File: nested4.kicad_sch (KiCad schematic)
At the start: 3 parts, among them J2 54-00285

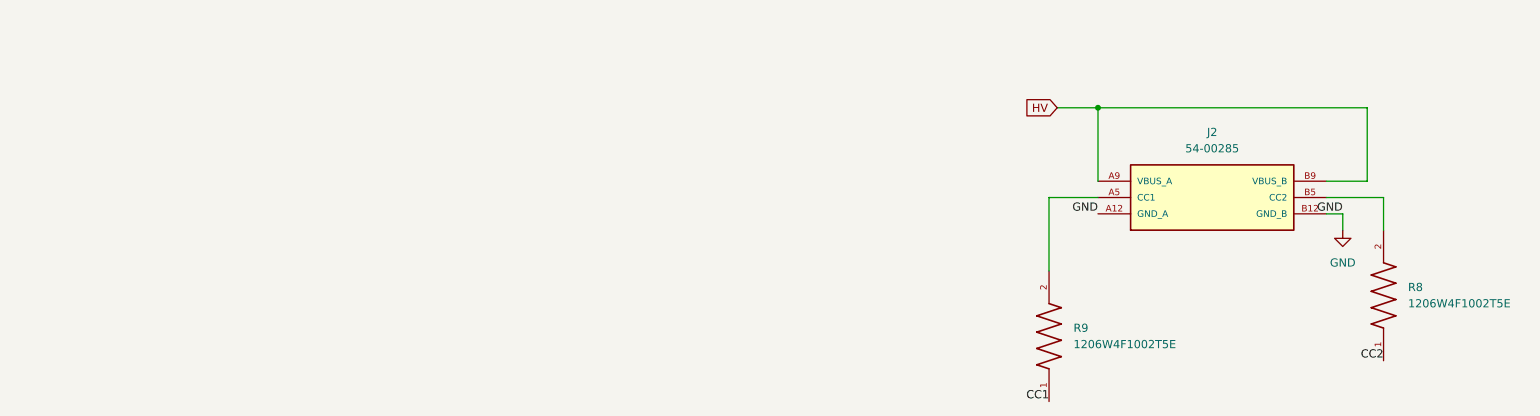
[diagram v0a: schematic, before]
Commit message: footprints added and usb cct finished
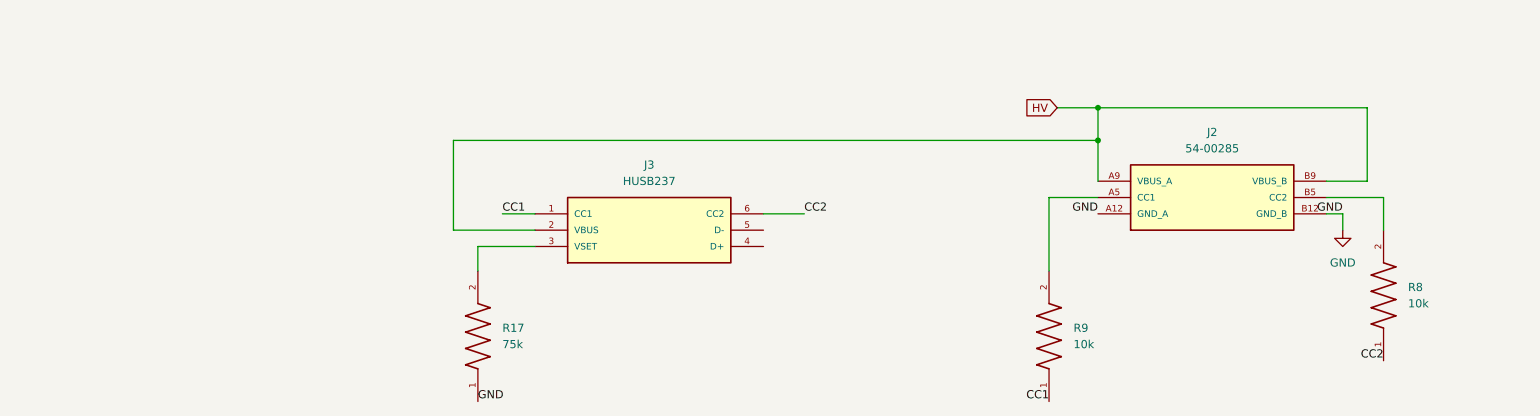
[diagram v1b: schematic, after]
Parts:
- added J3: HUSB237, Package_DFN_QFN:DFN-6-1EP_2x2mm_P0.65mm_EP1x1.6mm, symbol 54-00285[1]:54-00285
- added R17: 75k, Resistor_SMD:R_1206_3216Metric_Pad1.30x1.75mm_HandSolder, symbol 1206W4F1002T5E[1]:1206W4F1002T5E
- J2: footprint 54-00285:TENSILITY_54-00285 -> Connector_USB:USB_C_Receptacle_HRO_TYPE-C-31-M-17
- R8: value 1206W4F1002T5E -> 10k; footprint 1206W4F1002T5E:RESC3115X65N -> Resistor_SMD:R_1206_3216Metric_Pad1.30x1.75mm_HandSolder
- R9: value 1206W4F1002T5E -> 10k
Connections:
- net CC1: now also J3.1 (CC1)
- net CC2: now also J3.6 (CC2)
- net GND: now also R17.1
- net HV: now also J3.2 (VBUS)
- new net: J3.3 (VSET), R17.2

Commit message: added LCSC numbers and finsihed footprints
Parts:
- J2: LCSC (none) -> C456012
- J3: LCSC (none) -> C22373734
- R17: LCSC (none) -> C23242
- R8, R9: LCSC (none) -> C17902
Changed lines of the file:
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@@
+			)
+		)
+		(property "LCSC" "C22373734"
+			(at 115.57 100.33 0)
+			(effects
+				(font
+					(size 1.27 1.27)
+				)
+				(hide yes)
 			)
 		)
@@
 			)
 		)
+		(property "LCSC" "C17902"
+			(at 177.8 96.52 90)
+			(effects
+				(font
+					(size 1.27 1.27)
+				)
+				(hide yes)
+			)
+		)
 		(pin "1"
 		)
@@
 			)
 		)
+		(property "LCSC" "C456012"
+			(at 203.2 74.93 0)
+			(effects
+				(font
+					(size 1.27 1.27)
+				)
+				(hide yes)
+			)
+		)
 		(pin "B9"
 		)
@@
 			)
 		)
+		(property "LCSC" "C17902"
+			(at 229.87 90.17 90)
+			(effects
+				(font
+					(size 1.27 1.27)
+				)
+				(hide yes)
+			)
+		)
 		(pin "1"
 		)
@@
 				(hide yes)
 			)
+		)
+		(property "LCSC" "C23242"
+			(at 88.9 96.52 90)
+			(effects
+				(font
+					(size 1.27 1.27)
+				)
+				(hide yes)
+			)

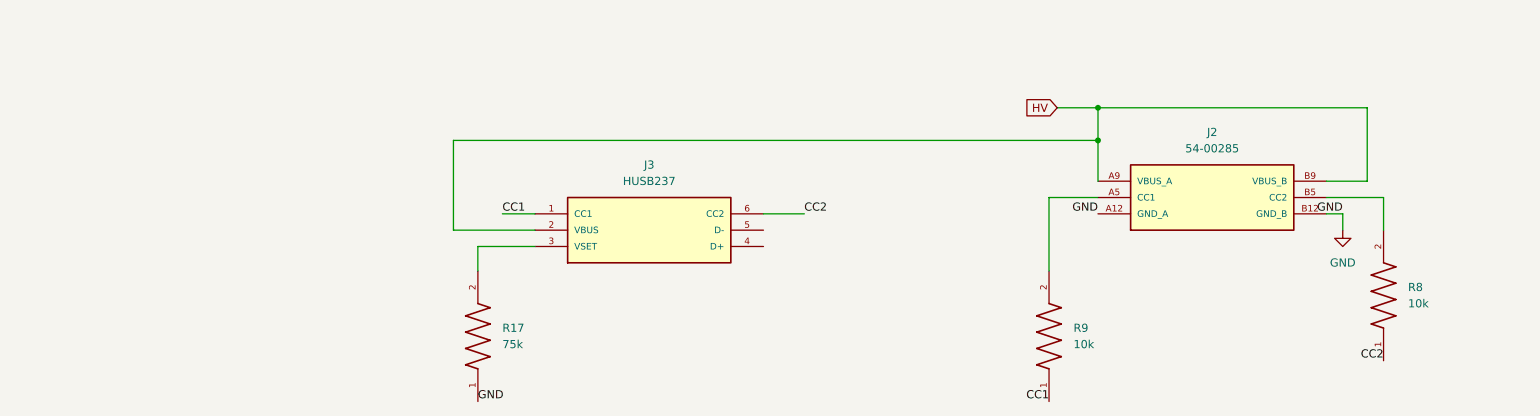
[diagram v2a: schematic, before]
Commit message: Removed old backups and updated KiCad files
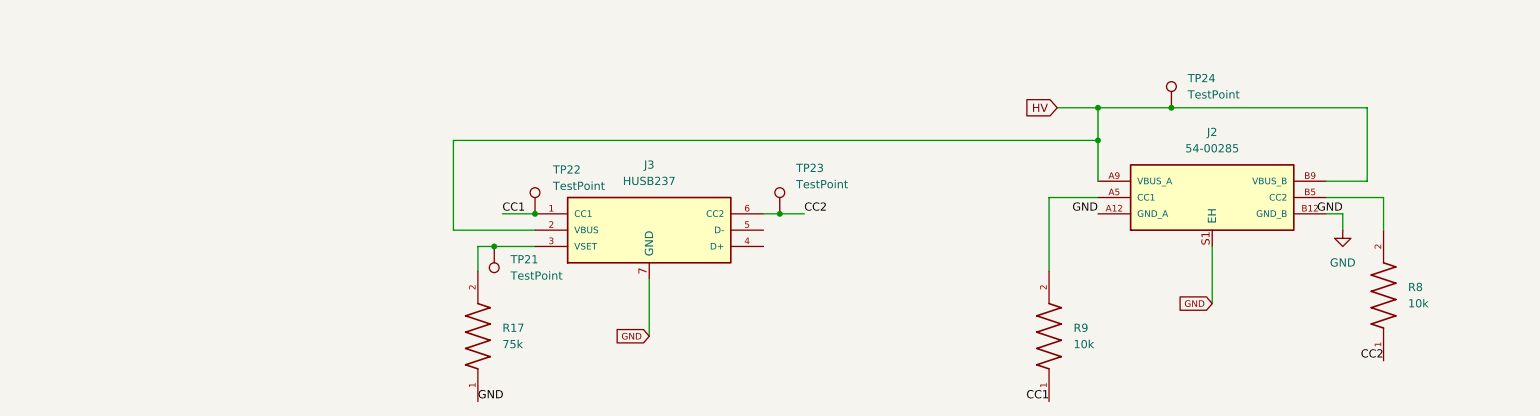
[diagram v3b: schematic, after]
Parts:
- added TP21, TP22, TP23, TP24: TestPoint, TestPoint:TestPoint_Pad_1.0x1.0mm, symbol Connector:TestPoint
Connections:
- net CC1: now also TP22.1
- net CC2: now also TP23.1
- net GND: now also J2.S1 (EH), J3.7 (GND)
- net HV: now also TP24.1
- net at J3.3 (VSET), R17.2: now also TP21.1

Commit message: Removed old backups and updated KiCad files
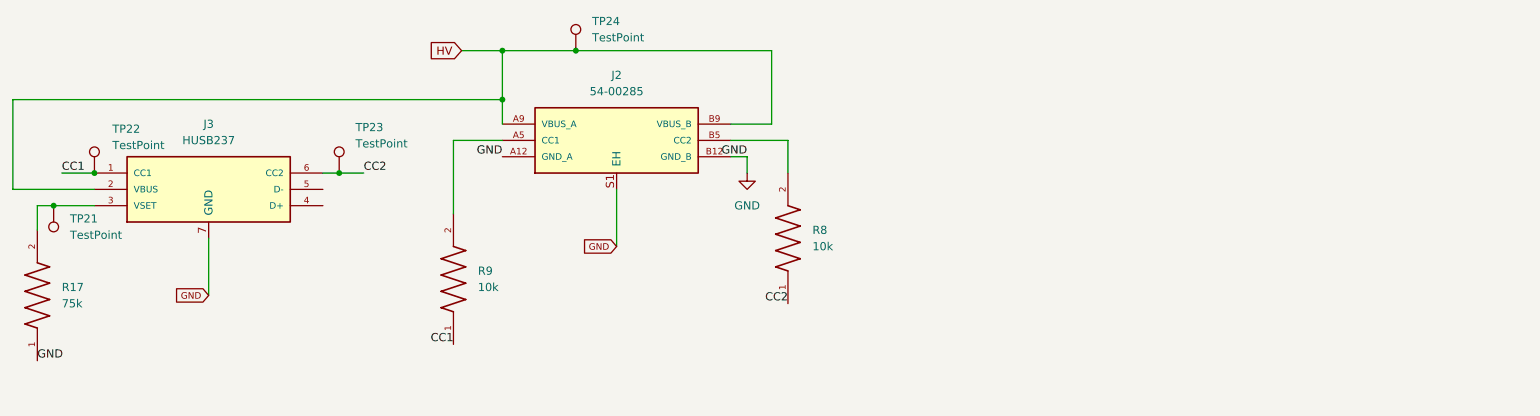
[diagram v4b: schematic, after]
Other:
- title: (none) -> MICRO-MOUSE POWER SUBSYSTEM
- moved on the sheet: J2, J3, R17, R8, R9, TP21, TP22, TP23, TP24
